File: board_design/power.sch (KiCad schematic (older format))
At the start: 12 parts, among them Q1 2N3904, Q2 IRFU9024NPBF, Q3 2N3904, U2 AS393P-E1, U3 R-78E5.0-0.5

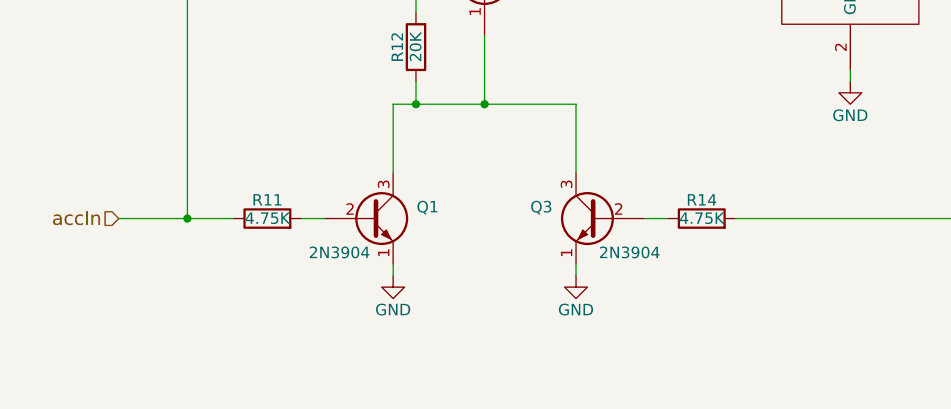
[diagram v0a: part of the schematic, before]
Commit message: WIP commit before redoing layout for 0.5mm bit and before adding microphone port.
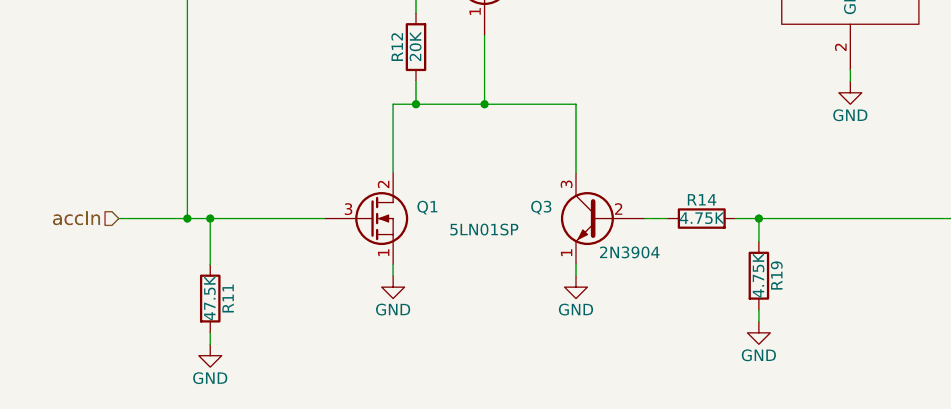
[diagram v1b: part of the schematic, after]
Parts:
- removed Q1: 2N3904, TO_SOT_Packages_THT:TO-92_Molded_Wide_Oval, symbol 2N3904
- added Q1: 5LN01SP, TO_SOT_Packages_THT:TO-92_Molded_Wide_Oval, symbol 5LN01SP
- added R19: 4.75K, Resistors_ThroughHole:Resistor_Horizontal_RM10mm, symbol R
- R11: value 4.75K -> 47.5K; MFP MFR-25FBF52-4K75 -> MFR-25FBF52-47K5
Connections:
- net GND: now also R11.2, Q1.1 (S), R19.2
- net accIn: now also Q1.3 (G)
- net holdPowerOnIn: now also R19.1
- net at Q2.1 (G), Q3.3 (C), R12.1: now also Q1.2 (D)
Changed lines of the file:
@@
 	1    0    0    -1
 $EndComp
-Wire Wire Line
-	3100 2800 4000 2800
-$Comp
-L GND #PWR011
+$Comp
+L GND #PWR012
 U 1 1 56F112AE
 P 4500 3300
-F 0 "#PWR011" H 4500 3050 50  0001 C CNN
+F 0 "#PWR012" H 4500 3050 50  0001 C CNN
 F 1 "GND" H 4500 3150 50  0000 C CNN
 F 2 "" H 4500 3300 50  0000 C CNN
@@
 	1    0    0    -1
 $EndComp
-Wire Wire Line
-	4500 3250 4500 3300
 $Comp
 L 1N4004 D1
@@
 	-1   0    0    1
 $EndComp
-Wire Wire Line
-	2500 2800 2700 2800
 Text HLabel 1300 2800 0    60   Input ~ 0
 battIn
 Text HLabel 1300 3900 0    60   Input ~ 0
 accIn
-Wire Wire Line
-	1300 2800 2200 2800
-$Comp
-L 2N3904 Q1
-U 1 1 56F11657
-P 2400 3900
-F 0 "Q1" H 2700 3950 50  0000 R CNN
-F 1 "2N3904" H 2400 3750 50  0000 R CNN
-F 2 "TO_SOT_Packages_THT:TO-92_Molded_Wide_Oval" H 2600 4000 50  0001 C CNN
-F 3 "" H 2400 3900 50  0000 C CNN
-F 4 "On Semiconductor" H 3500 1900 60  0001 C CNN "MFN"
-F 5 "2N3904" H 3500 1900 60  0001 C CNN "MFP"
-	1    2400 3900
-	1    0    0    -1
-$EndComp
-Wire Wire Line
-	2500 3700 2500 3400
-Wire Wire Line
-	2500 3400 3300 3400
-$Comp
-L R R11
-U 1 1 56F11799
-P 1950 3900
-F 0 "R11" V 2030 3900 50  0000 C CNN
-F 1 "4.75K" V 1950 3900 50  0000 C CNN
-F 2 "Resistors_ThroughHole:Resistor_Horizontal_RM10mm" V 1880 3900 50  0001 C CNN
-F 3 "" H 1950 3900 50  0000 C CNN
-F 4 "Yageo" V 2300 1600 60  0001 C CNN "MFN"
-F 5 "MFR-25FBF52-4K75" V 2300 1600 60  0001 C CNN "MFP"
-	1    1950 3900
-	0    -1   -1   0
-$EndComp
-Wire Wire Line
-	2100 3900 2200 3900
-Wire Wire Line
-	1300 3900 1800 3900
-$Comp
-L GND #PWR012
+$Comp
+L GND #PWR013
 U 1 1 56F118B7
 P 2500 4150
-F 0 "#PWR012" H 2500 3900 50  0001 C CNN
+F 0 "#PWR013" H 2500 3900 50  0001 C CNN
 F 1 "GND" H 2500 4000 50  0000 C CNN
 F 2 "" H 2500 4150 50  0000 C CNN
@@
 	1    0    0    -1
 $EndComp
-Wire Wire Line
-	2500 4100 2500 4150
 $Comp
 L 2N3904 Q3
@@
 	-1   0    0    -1
 $EndComp
-Wire Wire Line
-	3300 3400 3300 3700
-Wire Wire Line
-	2900 3400 2900 3100
-Connection ~ 2900 3400
-$Comp
-L GND #PWR013
+$Comp
+L GND #PWR014
 U 1 1 56F11AD9
 P 3300 4150
-F 0 "#PWR013" H 3300 3900 50  0001 C CNN
+F 0 "#PWR014" H 3300 3900 50  0001 C CNN
 F 1 "GND" H 3300 4000 50  0000 C CNN
 F 2 "" H 3300 4150 50  0000 C CNN
@@
 	1    0    0    -1
 $EndComp
-Wire Wire Line
-	3300 4100 3300 4150
 $Comp
 L R R14
@@
 	0    -1   -1   0
 $EndComp
-Wire Wire Line
-	3600 3900 3700 3900
-Wire Wire Line
-	2600 3300 2600 3400
-Connection ~ 2600 3400
-Wire Wire Line
-	2600 3000 2600 2800
-Connection ~ 2600 2800
 $Comp
 L CP C11
@@
 $EndComp
 $Comp
-L GND #PWR014
+L GND #PWR015
 U 1 1 56F12285
 P 5200 3250
-F 0 "#PWR014" H 5200 3000 50  0001 C CNN
+F 0 "#PWR015" H 5200 3000 50  0001 C CNN
 F 1 "GND" H 5200 3100 50  0000 C CNN
 F 2 "" H 5200 3250 50  0000 C CNN
@@
 	1    0    0    -1
 $EndComp
-Wire Wire Line
-	5200 3200 5200 3250
-Wire Wire Line
-	5000 2800 5600 2800
-Wire Wire Line
-	5200 2800 5200 2900
-Wire Wire Line
-	3300 2800 3300 800
-Wire Wire Line
-	3300 800  5600 800
-Connection ~ 3300 2800
 Text HLabel 5600 800  2    60   Output ~ 0
 SW12VOut
 Text HLabel 5600 2800 2    60   Output ~ 0
 5VOut
-Connection ~ 5200 2800
 Text HLabel 5600 3900 2    60   Input ~ 0
 holdPowerOnIn
-Wire Wire Line
-	5600 3900 4000 3900
 $Comp
 L AS393P-E1 U2
@@
 $EndComp
 $Comp
-L GND #PWR015
+L GND #PWR016
 U 1 1 56F126D5
 P 4300 1950
-F 0 "#PWR015" H 4300 1700 50  0001 C CNN
+F 0 "#PWR016" H 4300 1700 50  0001 C CNN
 F 1 "GND" H 4300 1800 50  0000 C CNN
 F 2 "" H 4300 1950 50  0000 C CNN
@@
 	1    0    0    -1
 $EndComp
-Wire Wire Line
-	4300 1900 4300 1950
 Text HLabel 5500 1600 2    60   Input ~ 0
 accSenseOut
@@
 	0    -1   -1   0
 $EndComp
-Wire Wire Line
-	4100 1700 3800 1700
-Wire Wire Line
-	3800 1200 3800 1800
-Connection ~ 3800 1700
-$Comp
-L GND #PWR016
+$Comp
+L GND #PWR017
 U 1 1 56F12A3B
 P 3800 2150
-F 0 "#PWR016" H 3800 1900 50  0001 C CNN
+F 0 "#PWR017" H 3800 1900 50  0001 C CNN
 F 1 "GND" H 3800 2000 50  0000 C CNN
 F 2 "" H 3800 2150 50  0000 C CNN
@@
 	1    0    0    -1
 $EndComp
-Wire Wire Line
-	3800 2100 3800 2150
-Wire Wire Line
-	4300 800  4300 1300
-Wire Wire Line
-	4700 1600 5500 1600
-Connection ~ 4300 800
-Connection ~ 4300 1200
-Wire Wire Line
-	4300 1200 4200 1200
-Wire Wire Line
-	3900 1200 3800 1200
-Wire Wire Line
-	4100 1500 1600 1500
-Wire Wire Line
-	1600 1500 1600 3900
-Connection ~ 1600 3900
 $Comp
 L R R12
@@
 	0    1    -1   0
 $EndComp
+$Comp
+L R R19
+U 1 1 5704874F
+P 4100 4150
+F 0 "R19" V 4180 4150 50  0000 C CNN
+F 1 "4.75K" V 4100 4150 50  0000 C CNN
+F 2 "Resistors_ThroughHole:Resistor_Horizontal_RM10mm" V 4030 4150 50  0001 C CNN
+F 3 "" H 4100 4150 50  0000 C CNN
+F 4 "Yageo" V 2550 1850 60  0001 C CNN "MFN"
+F 5 "MFR-25FBF52-4K75" V 2550 1850 60  0001 C CNN "MFP"
+	1    4100 4150
+	1    0    0    -1
+$EndComp
+$Comp
+L GND #PWR018
+U 1 1 57048826
+P 4100 4350
+F 0 "#PWR018" H 4100 4100 50  0001 C CNN
+F 1 "GND" H 4100 4200 50  0000 C CNN
+F 2 "" H 4100 4350 50  0000 C CNN
+F 3 "" H 4100 4350 50  0000 C CNN
+	1    4100 4350
+	1    0    0    -1
+$EndComp
+$Comp
+L R R11
+U 1 1 57048CAE
+P 1700 4250
+F 0 "R11" V 1780 4250 50  0000 C CNN
+F 1 "47.5K" V 1700 4250 50  0000 C CNN
+F 2 "Resistors_ThroughHole:Resistor_Horizontal_RM10mm" V 1630 4250 50  0001 C CNN
+F 3 "" H 1700 4250 50  0000 C CNN
+F 4 "Yageo" V 200 3900 60  0001 C CNN "MFN"
+F 5 "MFR-25FBF52-47K5" V 200 3900 60  0001 C CNN "MFP"
+	1    1700 4250
+	1    0    0    -1
+$EndComp
+$Comp
+L GND #PWR019
+U 1 1 57048CB5
+P 1700 4450
+F 0 "#PWR019" H 1700 4200 50  0001 C CNN
+F 1 "GND" H 1700 4300 50  0000 C CNN
+F 2 "" H 1700 4450 50  0000 C CNN
+F 3 "" H 1700 4450 50  0000 C CNN
+	1    1700 4450
+	1    0    0    -1
+$EndComp
+$Comp
+L 5LN01SP Q1
+U 1 1 57048EF1
+P 2400 3900
+F 0 "Q1" H 2700 3950 50  0000 R CNN
+F 1 "5LN01SP" H 3050 3850 50  0000 R CNN
+F 2 "TO_SOT_Packages_THT:TO-92_Molded_Wide_Oval" H 2600 4000 50  0001 C CNN
+F 3 "" H 2400 3900 50  0000 C CNN
+	1    2400 3900
+	1    0    0    -1
+$EndComp
+Wire Wire Line
+	3100 2800 4000 2800
+Wire Wire Line
+	4500 3250 4500 3300
+Wire Wire Line
+	2500 2800 2700 2800
+Wire Wire Line
+	1300 2800 2200 2800
+Wire Wire Line
+	2500 3700 2500 3400
+Wire Wire Line
+	2500 3400 3300 3400
+Wire Wire Line
+	2500 4100 2500 4150
+Wire Wire Line
+	3300 3400 3300 3700
+Wire Wire Line
+	2900 3400 2900 3100
+Connection ~ 2900 3400
+Wire Wire Line
+	3300 4100 3300 4150
+Wire Wire Line
+	3600 3900 3700 3900
+Wire Wire Line
+	2600 3300 2600 3400
+Connection ~ 2600 3400
+Wire Wire Line
+	2600 3000 2600 2800
+Connection ~ 2600 2800
+Wire Wire Line
+	5200 3200 5200 3250
+Wire Wire Line
+	5000 2800 5600 2800
+Wire Wire Line
+	5200 2800 5200 2900
+Wire Wire Line
+	3300 2800 3300 800
+Wire Wire Line
+	3300 800  5600 800
+Connection ~ 3300 2800
+Connection ~ 5200 2800
+Wire Wire Line
+	5600 3900 4000 3900
+Wire Wire Line
+	4300 1900 4300 1950
+Wire Wire Line
+	4100 1700 3800 1700
+Wire Wire Line
+	3800 1200 3800 1800
+Connection ~ 3800 1700
+Wire Wire Line
+	3800 2100 3800 2150
+Wire Wire Line
+	4300 800  4300 1300
+Wire Wire Line
+	4700 1600 5500 1600
+Connection ~ 4300 800
+Connection ~ 4300 1200
+Wire Wire Line
+	4300 1200 4200 1200
+Wire Wire Line
+	3900 1200 3800 1200
+Wire Wire Line
+	4100 1500 1600 1500
+Wire Wire Line
+	1600 1500 1600 3900
 Wire Wire Line
 	3100 2700 3150 2700
@@
 	3150 2700 3150 2800
 Connection ~ 3150 2800
+Wire Wire Line
+	4100 3900 4100 4000
+Connection ~ 4100 3900
+Wire Wire Line
+	4100 4300 4100 4350
+Wire Wire Line
+	1700 4400 1700 4450
+Wire Wire Line
+	1700 3900 1700 4100
+Wire Wire Line
+	1300 3900 2200 3900
+Connection ~ 1600 3900
+Connection ~ 1700 3900
 $EndSCHEMATC
